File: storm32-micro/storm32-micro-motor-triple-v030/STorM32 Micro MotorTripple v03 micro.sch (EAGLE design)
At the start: 32 parts, among them IC1 STM32F10XTXU6, IC3 DRV8839, IC4 DRV8839, IC5 DRV8839, IC6 DRV8839, IC7 DRV8839, Q1 RESONATORSMD

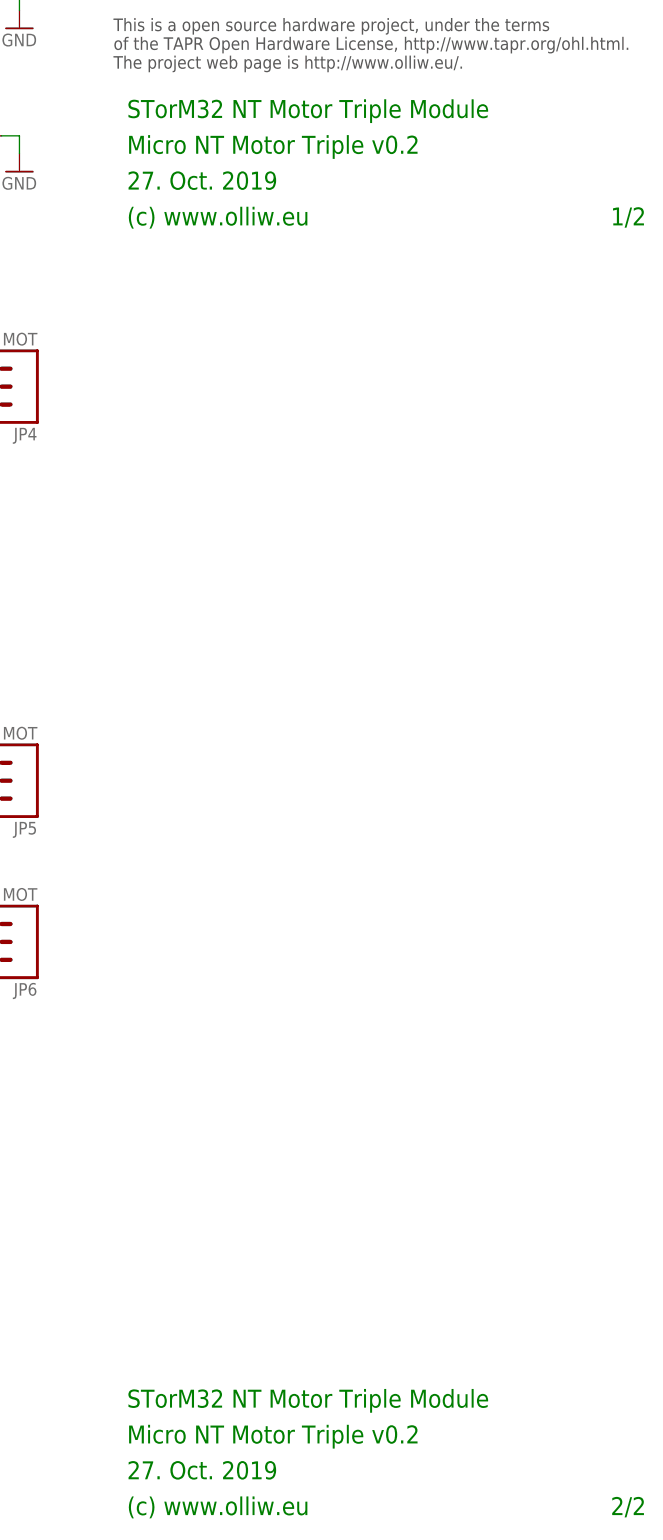
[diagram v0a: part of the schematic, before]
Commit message: release STorM32 Micro Motor Triple Board v0.30
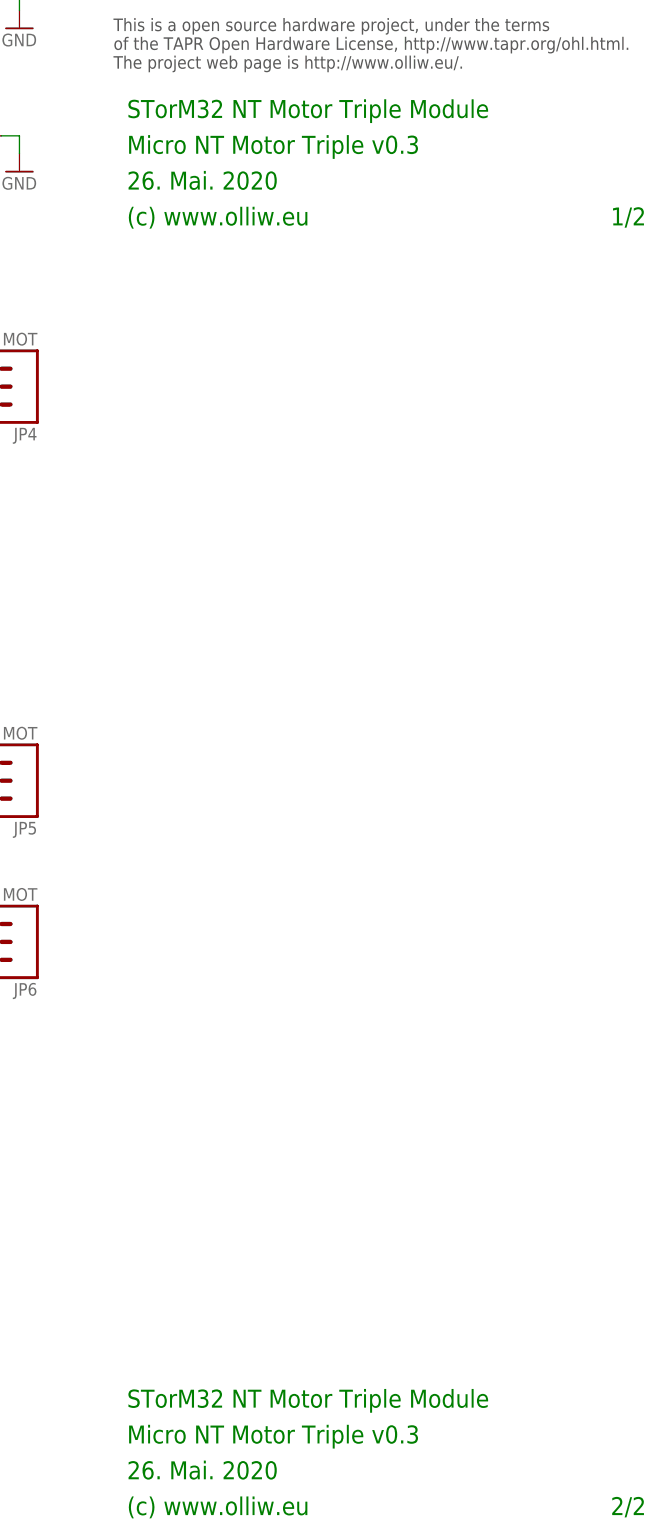
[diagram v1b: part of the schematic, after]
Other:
- note added: "26. Mai. 2020"
- note added: "Micro NT Motor Triple v0.3"
- note removed: "27. Oct. 2019"
- note removed: "Micro NT Motor Triple v0.2"
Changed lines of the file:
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@@
 <sheet>
 <plain>
-<text x="180.34" y="-38.1" size="2.54" layer="91">27. Oct. 2019</text>
+<text x="180.34" y="-38.1" size="2.54" layer="91">26. Mai. 2020</text>
 <text x="180.34" y="-43.18" size="2.54" layer="91">(c) www.olliw.eu</text>
 <text x="180.34" y="-27.94" size="2.54" layer="91">STorM32 NT Motor Triple Module</text>
-<text x="180.34" y="-33.02" size="2.54" layer="91">Micro NT Motor Triple v0.2</text>
+<text x="180.34" y="-33.02" size="2.54" layer="91">Micro NT Motor Triple v0.3</text>
 <text x="196.215" y="116.205" size="1.778" layer="97">T-STorM32 NT
 Motor Module Mini for three motors, without encoder</text>
@@
 The project web page is http://www.olliw.eu/.</text>
 <text x="180.34" y="-210.82" size="2.54" layer="91">STorM32 NT Motor Triple Module</text>
-<text x="180.34" y="-215.9" size="2.54" layer="91">Micro NT Motor Triple v0.2</text>
-<text x="180.34" y="-220.98" size="2.54" layer="91">27. Oct. 2019</text>
+<text x="180.34" y="-215.9" size="2.54" layer="91">Micro NT Motor Triple v0.3</text>
+<text x="180.34" y="-220.98" size="2.54" layer="91">26. Mai. 2020</text>
 <text x="180.34" y="-226.06" size="2.54" layer="91">(c) www.olliw.eu</text>
 <text x="248.92" y="-43.18" size="2.54" layer="91">1/2</text>
